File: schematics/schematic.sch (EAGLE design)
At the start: 22 parts, among them U1 TSR_1-2450

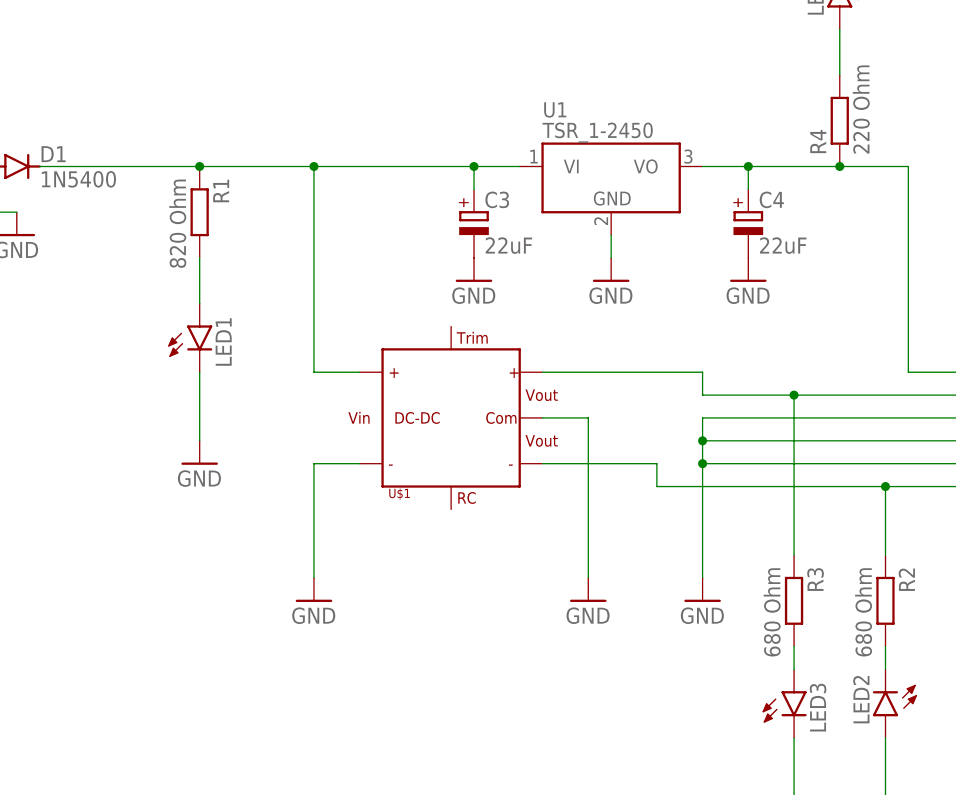
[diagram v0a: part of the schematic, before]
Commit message: replaced dc dc converter with smaller 15W version
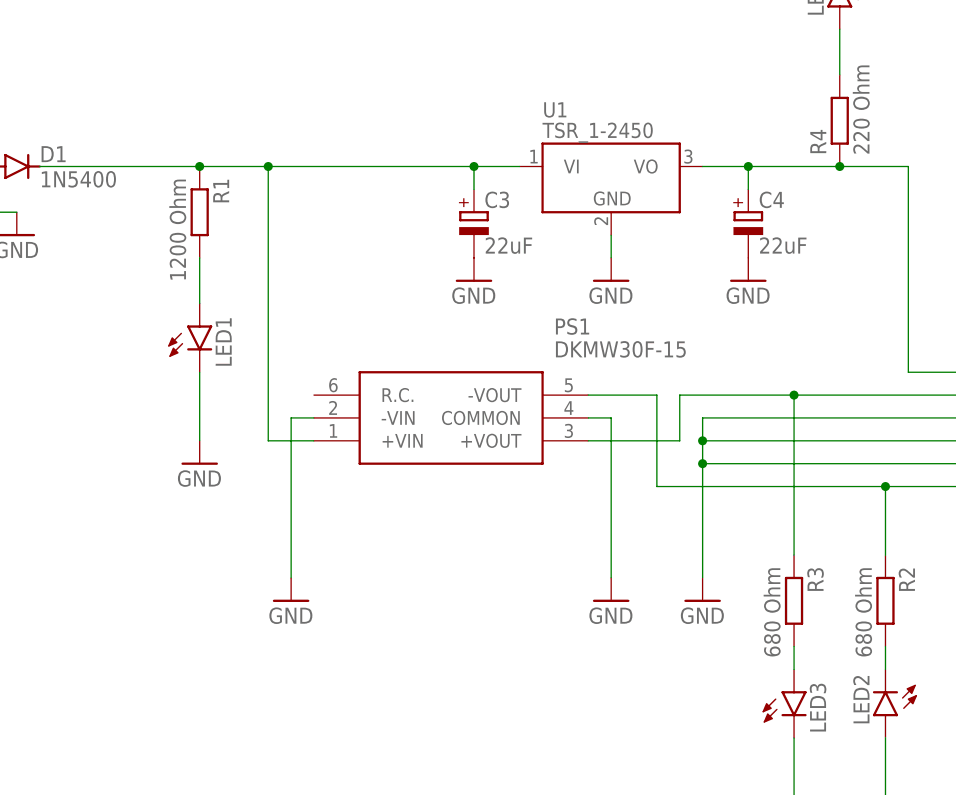
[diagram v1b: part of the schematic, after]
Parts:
- removed U$1: (no value), dk30a:DKA30"
- added PS1: DKMW30F-15, DKMW30F-15:DKMW30F-15
- R1: value 820 Ohm -> 1200 Ohm
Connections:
- net +12V: now also PS1.+VOUT; no longer U$1.+VOUT
- net -12V: now also PS1.-VOUT; no longer U$1.-VOUT
- net GND: now also PS1.-VIN, PS1.COMMON; no longer U$1.-VIN, U$1.COM
- net VI: now also PS1.+VIN; no longer U$1.+VIN
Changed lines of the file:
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@@
 </groups>
 <parts>
-<part name="U$1" library="dk30a" deviceset="DKA30" device="&quot;"/>
 <part name="GND1" library="supply1" library_urn="urn:adsk.eagle:library:371" deviceset="GND" device=""/>
 <part name="D1" library="diode" library_urn="urn:adsk.eagle:library:210" deviceset="1N5400" device="" package3d_urn="urn:adsk.eagle:package:43365/2"/>
@@
 <part name="LED1" library="led" library_urn="urn:adsk.eagle:library:259" deviceset="LED" device="3MM" package3d_urn="urn:adsk.eagle:package:15797/1"/>
 <part name="GND8" library="supply1" library_urn="urn:adsk.eagle:library:371" deviceset="GND" device=""/>
-<part name="R1" library="rcl" library_urn="urn:adsk.eagle:library:334" deviceset="R-EU_" device="0207/10" package3d_urn="urn:adsk.eagle:package:23491/2" value="820 Ohm"/>
+<part name="R1" library="rcl" library_urn="urn:adsk.eagle:library:334" deviceset="R-EU_" device="0207/10" package3d_urn="urn:adsk.eagle:package:23491/2" value="1200 Ohm"/>
 <part name="LED2" library="led" library_urn="urn:adsk.eagle:library:259" deviceset="LED" device="3MM" package3d_urn="urn:adsk.eagle:package:15797/1"/>
 <part name="GND9" library="supply1" library_urn="urn:adsk.eagle:library:371" deviceset="GND" device=""/>
@@
 <part name="SV9" library="con-lsta" library_urn="urn:adsk.eagle:library:161" deviceset="FE08-2" device="" package3d_urn="urn:adsk.eagle:package:8174/1"/>
 <part name="X1" library="con-wago-500" library_urn="urn:adsk.eagle:library:195" deviceset="W237-4" device="" package3d_urn="urn:adsk.eagle:package:10695/1"/>
+<part name="PS1" library="DKMW30F-15" deviceset="DKMW30F-15" device=""/>
 </parts>
 <sheets>
@@
 </plain>
 <instances>
-<instance part="U$1" gate="G$1" x="66.04" y="68.58" smashed="yes">
-<attribute name="VALUE" x="59.055" y="61.595" size="1.016" layer="94" font="vector"/>
-<attribute name="NAME" x="59.055" y="59.69" size="1.016" layer="94" font="vector"/>
-</instance>
 <instance part="GND1" gate="1" x="17.78" y="88.9" smashed="yes">
 <attribute name="VALUE" x="15.24" y="86.36" size="1.778" layer="96"/>
@@
 <attribute name="VALUE" x="20.32" y="94.2086" size="1.778" layer="96"/>
 </instance>
-<instance part="GND2" gate="1" x="50.8" y="48.26" smashed="yes">
-<attribute name="VALUE" x="48.26" y="45.72" size="1.778" layer="96"/>
+<instance part="GND2" gate="1" x="48.26" y="48.26" smashed="yes">
+<attribute name="VALUE" x="45.72" y="45.72" size="1.778" layer="96"/>
 </instance>
 <instance part="U1" gate="G$1" x="83.82" y="96.52" smashed="yes">
@@
 <attribute name="VALUE" x="91.44" y="45.72" size="1.778" layer="96"/>
 </instance>
-<instance part="GND5" gate="1" x="81.28" y="48.26" smashed="yes">
-<attribute name="VALUE" x="78.74" y="45.72" size="1.778" layer="96"/>
+<instance part="GND5" gate="1" x="83.82" y="48.26" smashed="yes">
+<attribute name="VALUE" x="81.28" y="45.72" size="1.778" layer="96"/>
 </instance>
 <instance part="GND6" gate="1" x="68.58" y="83.82" smashed="yes">
@@
 <attribute name="VALUE" x="-2.54" y="82.677" size="1.778" layer="96"/>
 <attribute name="NAME" x="0" y="87.249" size="1.778" layer="95" rot="R180"/>
+</instance>
+<instance part="PS1" gate="G$1" x="50.8" y="71.12" smashed="yes">
+<attribute name="NAME" x="77.47" y="78.74" size="1.778" layer="95" align="center-left"/>
+<attribute name="VALUE" x="77.47" y="76.2" size="1.778" layer="96" align="center-left"/>
 </instance>
 </instances>
@@
 <wire x1="5.08" y1="91.44" x2="5.08" y2="86.36" width="0.1524" layer="91"/>
 <junction x="5.08" y="91.44"/>
-</segment>
-<segment>
-<pinref part="U$1" gate="G$1" pin="-VIN"/>
-<pinref part="GND2" gate="1" pin="GND"/>
-<wire x1="55.88" y1="63.5" x2="50.8" y2="63.5" width="0.1524" layer="91"/>
-<wire x1="50.8" y1="63.5" x2="50.8" y2="50.8" width="0.1524" layer="91"/>
 </segment>
 <segment>
@@
 </segment>
 <segment>
-<pinref part="GND5" gate="1" pin="GND"/>
-<wire x1="81.28" y1="50.8" x2="81.28" y2="68.58" width="0.1524" layer="91"/>
-<pinref part="U$1" gate="G$1" pin="COM"/>
-<wire x1="81.28" y1="68.58" x2="76.2" y2="68.58" width="0.1524" layer="91"/>
-</segment>
-<segment>
 <pinref part="LED1" gate="G$1" pin="C"/>
 <pinref part="GND8" gate="1" pin="GND"/>
@@
 <pinref part="GND7" gate="1" pin="GND"/>
 <pinref part="C4" gate="G$1" pin="-"/>
+</segment>
+<segment>
+<pinref part="GND5" gate="1" pin="GND"/>
+<pinref part="PS1" gate="G$1" pin="COMMON"/>
+<wire x1="83.82" y1="50.8" x2="83.82" y2="68.58" width="0.1524" layer="91"/>
+<wire x1="83.82" y1="68.58" x2="81.28" y2="68.58" width="0.1524" layer="91"/>
+</segment>
+<segment>
+<pinref part="PS1" gate="G$1" pin="-VIN"/>
+<pinref part="GND2" gate="1" pin="GND"/>
+<wire x1="50.8" y1="68.58" x2="48.26" y2="68.58" width="0.1524" layer="91"/>
+<wire x1="48.26" y1="68.58" x2="48.26" y2="50.8" width="0.1524" layer="91"/>
 </segment>
 </net>
@@
 <junction x="264.16" y="71.12"/>
 <junction x="279.4" y="71.12"/>
-<pinref part="U$1" gate="G$1" pin="+VOUT"/>
-<wire x1="76.2" y1="73.66" x2="93.98" y2="73.66" width="0.1524" layer="91"/>
-<wire x1="93.98" y1="73.66" x2="93.98" y2="71.12" width="0.1524" layer="91"/>
-<wire x1="93.98" y1="71.12" x2="104.14" y2="71.12" width="0.1524" layer="91"/>
+<wire x1="91.44" y1="71.12" x2="104.14" y2="71.12" width="0.1524" layer="91"/>
 <pinref part="R3" gate="G$1" pin="1"/>
 <wire x1="104.14" y1="53.34" x2="104.14" y2="71.12" width="0.1524" layer="91"/>
@@
 <junction x="187.96" y="71.12"/>
 <junction x="104.14" y="71.12"/>
+<wire x1="91.44" y1="71.12" x2="91.44" y2="66.04" width="0.1524" layer="91"/>
+<pinref part="PS1" gate="G$1" pin="+VOUT"/>
+<wire x1="91.44" y1="66.04" x2="81.28" y2="66.04" width="0.1524" layer="91"/>
 </segment>
 </net>
 <net name="VI" class="0">
 <segment>
-<pinref part="U$1" gate="G$1" pin="+VIN"/>
-<wire x1="50.8" y1="96.52" x2="50.8" y2="73.66" width="0.1524" layer="91"/>
-<wire x1="50.8" y1="73.66" x2="55.88" y2="73.66" width="0.1524" layer="91"/>
 <pinref part="U1" gate="G$1" pin="VI"/>
 <wire x1="73.66" y1="96.52" x2="68.58" y2="96.52" width="0.1524" layer="91"/>
 <pinref part="D1" gate="1" pin="C"/>
-<wire x1="68.58" y1="96.52" x2="50.8" y2="96.52" width="0.1524" layer="91"/>
+<wire x1="68.58" y1="96.52" x2="45.72" y2="96.52" width="0.1524" layer="91"/>
+<wire x1="45.72" y1="96.52" x2="38.1" y2="96.52" width="0.1524" layer="91"/>
 <wire x1="20.32" y1="96.52" x2="38.1" y2="96.52" width="0.1524" layer="91"/>
-<junction x="50.8" y="96.52"/>
-<wire x1="38.1" y1="96.52" x2="50.8" y2="96.52" width="0.1524" layer="91"/>
 <wire x1="68.58" y1="93.98" x2="68.58" y2="96.52" width="0.1524" layer="91"/>
 <junction x="68.58" y="96.52"/>
@@
 <junction x="38.1" y="96.52"/>
 <pinref part="C3" gate="G$1" pin="+"/>
+<pinref part="PS1" gate="G$1" pin="+VIN"/>
+<wire x1="50.8" y1="66.04" x2="45.72" y2="66.04" width="0.1524" layer="91"/>
+<wire x1="45.72" y1="66.04" x2="45.72" y2="96.52" width="0.1524" layer="91"/>
+<junction x="45.72" y="96.52"/>
 </segment>
 </net>
@@
 <net name="-12V" class="0">
 <segment>
-<pinref part="U$1" gate="G$1" pin="-VOUT"/>
 <pinref part="R2" gate="G$1" pin="1"/>
 <wire x1="114.3" y1="53.34" x2="114.3" y2="60.96" width="0.1524" layer="91"/>
 <wire x1="114.3" y1="60.96" x2="88.9" y2="60.96" width="0.1524" layer="91"/>
-<wire x1="88.9" y1="60.96" x2="88.9" y2="63.5" width="0.1524" layer="91"/>
-<wire x1="88.9" y1="63.5" x2="76.2" y2="63.5" width="0.1524" layer="91"/>
 <label x="137.16" y="60.96" size="1.778" layer="95"/>
 <pinref part="SV1" gate="G$1" pin="2"/>
@@
 <junction x="114.3" y="60.96"/>
 <junction x="187.96" y="60.96"/>
-</segment>
-</net>
+<wire x1="88.9" y1="60.96" x2="88.9" y2="71.12" width="0.1524" layer="91"/>
+<pinref part="PS1" gate="G$1" pin="-VOUT"/>
+<wire x1="88.9" y1="71.12" x2="81.28" y2="71.12" width="0.1524" layer="91"/>
+</segment>
+</net>
